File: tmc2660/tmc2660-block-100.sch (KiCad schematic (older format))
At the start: 18 parts, among them J100 0R, M100 Mount, M101 Mount, P100 Motor, U100 TMC2660

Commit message: Wire up quad according to new MISO/MOSI sequence.
- Also, add basic STEP/DIR and a capacitor.
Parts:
- added C?: 100u, Capacitors_THT:CP_Radial_D10.0mm_P5.00mm, symbol device:CP
- renumbered C101 to C100, C100 to C101, C103 to C102, C102 to C103, C106 to C105, C107 to C106, C105 to C107, R101 to R100, R100 to R101, R103 to R102, R102 to R103
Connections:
- net labels added: START_MOSI
- net labels removed: GLOBAL_MISO
- wire segments 51 -> 50
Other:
- note added: "Jumper on\nhighest popuplated"
- note removed: "Optional"
- moved on the sheet: J100
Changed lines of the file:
@@
 EESchema Schematic File Version 4
-LIBS:tmc2660-mono-cache
+LIBS:tmc2660-quad-cache
 EELAYER 26 0
 EELAYER END
 $Descr A4 11693 8268
 encoding utf-8
-Sheet 2 2
+Sheet 2 5
 Title ""
 Date ""
@@
 $EndDescr
 $Comp
-L device:C C102
+L device:C C103
 U 1 1 5A0CA5B9
 P 4250 2250
-F 0 "C102" H 4275 2350 50  0000 L CNN
+F 0 "C103" H 4275 2350 50  0000 L CNN
 F 1 "10u" H 4275 2150 50  0000 L CNN
 F 2 "Capacitors_SMD:C_1206" H 4288 2100 30  0001 C CNN
@@
 $EndComp
 $Comp
-L device:C C103
+L device:C C102
 U 1 1 5A0CA5C0
 P 4250 3100
-F 0 "C103" H 4275 3200 50  0000 L CNN
+F 0 "C102" H 4275 3200 50  0000 L CNN
 F 1 "10u" H 4275 3000 50  0000 L CNN
 F 2 "Capacitors_SMD:C_1206" H 4288 2950 30  0001 C CNN
@@
 $EndComp
 $Comp
-L device:C C106
+L device:C C105
 U 1 1 5A0CA5D3
 P 2900 1800
-F 0 "C106" H 2650 1900 50  0000 L CNN
+F 0 "C105" H 2650 1900 50  0000 L CNN
 F 1 "100n" H 2700 1700 50  0000 L CNN
 F 2 "Capacitors_SMD:C_0805" H 2938 1650 30  0001 C CNN
@@
 Connection ~ 3400 3150
 $Comp
-L device:R R102
+L device:R R103
 U 1 1 5A0CA5F8
 P 3550 2700
-F 0 "R102" V 3650 2700 50  0000 C CNN
+F 0 "R103" V 3650 2700 50  0000 C CNN
 F 1 "10R" V 3550 2700 50  0000 C CNN
 F 2 "Resistors_SMD:R_0603" V 3480 2700 30  0001 C CNN
@@
 $EndComp
 $Comp
-L device:R R103
+L device:R R102
 U 1 1 5A0CA5FF
 P 3550 3550
-F 0 "R103" V 3450 3550 50  0000 C CNN
+F 0 "R102" V 3450 3550 50  0000 C CNN
 F 1 "10R" V 3550 3550 50  0000 C CNN
 F 2 "Resistors_SMD:R_0603" V 3480 3550 30  0001 C CNN
@@
 $EndComp
 $Comp
-L device:C C107
+L device:C C106
 U 1 1 5A0CA648
 P 2250 3700
-F 0 "C107" H 1950 3700 50  0000 L CNN
+F 0 "C106" H 1950 3700 50  0000 L CNN
 F 1 "100n" H 2050 3600 50  0000 L CNN
 F 2 "Capacitors_SMD:C_0603" H 2288 3550 30  0001 C CNN
@@
 $EndComp
 Wire Wire Line
-	1500 2150 2350 2150
+	2050 2150 2350 2150
 Wire Wire Line
 	2350 3500 2300 3500
@@
 	2300 3500 2300 3550
 Wire Wire Line
-	2300 3550 2000 3550
+	2000 3550 2300 3550
 $Comp
 L power:GND #PWR0109
@@
 $EndComp
 $Comp
-L device:R R101
+L device:R R100
 U 1 1 5A0CA66C
 P 3950 3700
-F 0 "R101" V 3850 3650 50  0000 C CNN
+F 0 "R100" V 3850 3650 50  0000 C CNN
 F 1 "0.075" V 3950 3700 50  0000 C CNN
 F 2 "Resistors_SMD:R_2512" V 3880 3700 30  0001 C CNN
@@
 $EndComp
 $Comp
-L device:R R100
+L device:R R101
 U 1 1 5A0CA673
 P 3950 2850
-F 0 "R100" V 3850 2850 50  0000 C CNN
+F 0 "R101" V 3850 2850 50  0000 C CNN
 F 1 "0.075" V 3950 2850 50  0000 C CNN
 F 2 "Resistors_SMD:R_2512" V 3880 2850 30  0001 C CNN
@@
 	2250 2250 2350 2250
 $Comp
-L device:C_Small C100
+L device:C_Small C101
 U 1 1 5A0CA67B
 P 3950 2700
-F 0 "C100" V 3800 2600 50  0000 L CNN
+F 0 "C101" V 3800 2600 50  0000 L CNN
 F 1 "10n" V 3900 2750 50  0000 L CNN
 F 2 "Capacitors_SMD:C_0603" H 3988 2550 30  0001 C CNN
@@
 	3400 2450 3600 2450
 $Comp
-L device:C_Small C101
+L device:C_Small C100
 U 1 1 5A0CA683
 P 3950 3550
-F 0 "C101" V 4000 3600 50  0000 L CNN
+F 0 "C100" V 4000 3600 50  0000 L CNN
 F 1 "10n" V 4000 3350 50  0000 L CNN
 F 2 "Capacitors_SMD:C_0603" H 3988 3400 30  0001 C CNN
@@
 DIR
 Wire Wire Line
-	1250 2400 2350 2400
+	1850 2400 2350 2400
 Wire Wire Line
 	2350 2500 1250 2500
@@
 Connection ~ 3800 2700
 $Comp
-L device:CP C105
+L device:CP C107
 U 1 1 5A0CA6BD
 P 3500 1700
-F 0 "C105" H 3525 1800 50  0000 L CNN
+F 0 "C107" H 3525 1800 50  0000 L CNN
 F 1 "100u" H 3400 1900 50  0000 L CNN
 F 2 "Capacitors_THT:CP_Radial_D10.0mm_P5.00mm" H 3538 1550 30  0001 C CNN
@@
 	3200 1850 3500 1850
 Connection ~ 3350 1850
-Text Notes 1600 2350 0    60   ~ 0
-Optional
+Text Notes 600  2400 0    51   ~ 0
+Jumper on\nhighest popuplated
 Text HLabel 3750 1550 2    60   Input ~ 0
 VMot
@@
 Text HLabel 2000 3550 0    60   Input ~ 0
 VCC
-Text HLabel 1500 2150 0    60   Input ~ 0
+Text HLabel 2050 2150 0    60   Input ~ 0
 ~EN
 $Comp
 L device:R J100
 U 1 1 5A0CA6C8
-P 1400 2300
-F 0 "J100" V 1450 2100 50  0000 C CNN
-F 1 "0R" V 1400 2300 50  0000 C CNN
-F 2 "Resistors_SMD:R_0603" V 1330 2300 30  0001 C CNN
-F 3 "" H 1400 2300 30  0000 C CNN
-	1    1400 2300
-	0    -1   -1   0
-$EndComp
-Text HLabel 1250 2300 0    60   Input ~ 0
-GLOBAL_MISO
-Text HLabel 1250 2400 0    60   Input ~ 0
+P 1450 2350
+F 0 "J100" H 1550 2500 50  0000 C CNN
+F 1 "0R" V 1450 2350 50  0000 C CNN
+F 2 "Resistors_SMD:R_0603" V 1380 2350 30  0001 C CNN
+F 3 "" H 1450 2350 30  0000 C CNN
+	1    1450 2350
+	1    0    0    -1
+$EndComp
+Text HLabel 1250 2200 0    60   Input ~ 0
+START_MOSI
+Text HLabel 1850 2400 0    60   Input ~ 0
 MISO
-Wire Wire Line
-	1550 2300 1600 2300
-Wire Wire Line
-	1600 2300 1600 2400
-Connection ~ 1600 2400
 Text HLabel 1250 2500 0    60   Input ~ 0
 MOSI
@@
 	1    0    0    -1
 $EndComp
+Wire Wire Line
+	1250 2200 1450 2200
+Connection ~ 1450 2500
+$Comp
+L device:CP C?
+U 1 1 5A13AFA9
+P 950 650
+F 0 "C?" H 975 750 50  0000 L CNN
+F 1 "100u" H 850 850 50  0000 L CNN
+F 2 "Capacitors_THT:CP_Radial_D10.0mm_P5.00mm" H 988 500 30  0001 C CNN
+F 3 "" H 950 650 60  0000 C CNN
+	1    950  650
+	1    0    0    -1
+$EndComp

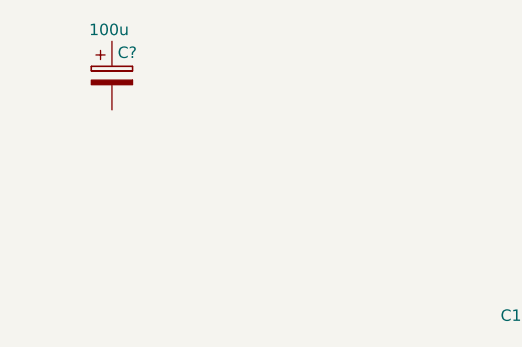
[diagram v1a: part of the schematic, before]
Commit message: Initial version of PCB with cloned template components.
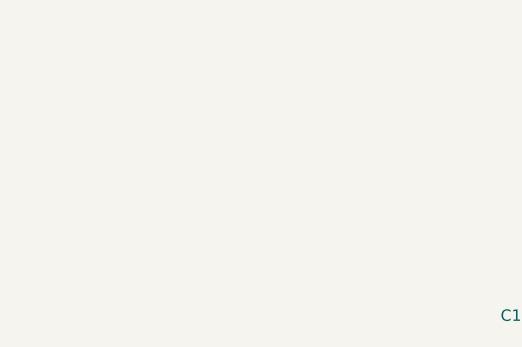
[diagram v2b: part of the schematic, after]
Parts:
- removed C?: 100u, Capacitors_THT:CP_Radial_D10.0mm_P5.00mm, symbol device:CP
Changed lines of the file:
@@
 	1250 2200 1450 2200
 Connection ~ 1450 2500
-$Comp
-L device:CP C?
-U 1 1 5A13AFA9
-P 950 650
-F 0 "C?" H 975 750 50  0000 L CNN
-F 1 "100u" H 850 850 50  0000 L CNN
-F 2 "Capacitors_THT:CP_Radial_D10.0mm_P5.00mm" H 988 500 30  0001 C CNN
-F 3 "" H 950 650 60  0000 C CNN
-	1    950  650
-	1    0    0    -1
-$EndComp
 $EndSCHEMATC

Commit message: Update tmc2660-quad with new template.
o Start out with a tmc2660-quad-baseline that is filled
  in with zones and tracks from the template.
o The separation from baseline and template allows faster
  updates later.
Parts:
- C102, C103: Voltage (none) -> 50V
- C104: footprint Capacitors_SMD:C_0805 -> Capacitors_SMD:C_0603; Voltage (none) -> 50V
- C105: footprint Capacitors_SMD:C_0805 -> Capacitors_SMD:C_0603; Voltage (none) -> 16V
- C106, C108: Voltage (none) -> 16V
- C107: value 100u -> 180u; footprint Capacitors_THT:CP_Radial_D10.0mm_P5.00mm -> Capacitors_THT:CP_Radial_D8.0mm_P3.50mm; DigiKey (none) -> 565-3911-ND; Voltage (none) -> 35V
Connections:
- net labels added: VHS
- wire segments 50 -> 44
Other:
- moved on the sheet: C100, C101, C102, C103, C105, P100, R100, R101, R102, R103

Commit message: Integrate grounded mounting hole.
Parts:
- C102, C103: DigiKey (none) -> 1276-6736-1-ND
- C104: footprint Capacitors_SMD:C_0603 -> Capacitors_SMD:C_0805; DigiKey (none) -> 1276-2450-2-ND
- C105, C106: footprint Capacitors_SMD:C_0603 -> Capacitors_SMD:C_0805; DigiKey (none) -> 1276-2450-2-ND; Voltage 16V -> >= 16V
- M101: footprint Mounting_Holes:MountingHole_2.7mm_M2.5 -> Mounting_Holes:MountingHole_2.7mm_M2.5_Pad; symbol Mechanical:Mounting_Hole -> Mechanical:Mounting_Hole_PAD
- R100, R101: Alternative 100mOhm (none) -> CRM2512-JX-R100ELFCT-ND; DigiKey (none) -> CSRN2512FK75L0CT-ND
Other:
- note added: "Sense Resistors alternatively\nalso with 100mOhm"
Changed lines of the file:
@@
 EESchema Schematic File Version 4
-LIBS:tmc2660-mono-cache
 EELAYER 26 0
 EELAYER END
@@
 F 3 "" H 4400 2300 60  0000 C CNN
 F 4 "50V" H 4400 2300 60  0001 C CNN "Voltage"
+F 5 "1276-6736-1-ND" H 4400 2300 60  0001 C CNN "DigiKey"
 	1    4400 2300
 	1    0    0    -1
@@
 F 3 "" H 4100 2300 60  0000 C CNN
 F 4 "50V" H 4100 2300 60  0001 C CNN "Voltage"
+F 5 "1276-6736-1-ND" H 4100 2300 60  0001 C CNN "DigiKey"
 	1    4100 2300
 	1    0    0    -1
@@
 F 0 "C105" H 2800 2000 50  0000 L CNN
 F 1 "100n" H 2700 1800 50  0000 L CNN
-F 2 "Capacitors_SMD:C_0603" H 2938 1550 30  0001 C CNN
+F 2 "Capacitors_SMD:C_0805" H 2938 1550 30  0001 C CNN
 F 3 "" H 2900 1700 60  0000 C CNN
-F 4 "16V" H 2900 1700 60  0001 C CNN "Voltage"
+F 4 ">= 16V" H 2900 1700 60  0001 C CNN "Voltage"
+F 5 "1276-2450-2-ND" H 2900 1700 60  0001 C CNN "DigiKey"
 	1    2900 1700
 	1    0    0    -1
@@
 F 0 "C104" H 3150 2000 50  0000 L CNN
 F 1 "100n" H 3150 1900 50  0000 L CNN
-F 2 "Capacitors_SMD:C_0603" H 3238 1550 30  0001 C CNN
+F 2 "Capacitors_SMD:C_0805" H 3238 1550 30  0001 C CNN
 F 3 "" H 3200 1700 60  0000 C CNN
 F 4 "50V" H 3200 1700 60  0001 C CNN "Voltage"
+F 5 "1276-2450-2-ND" H 3200 1700 60  0001 C CNN "DigiKey"
 	1    3200 1700
 	1    0    0    -1
@@
 F 0 "C106" H 1950 3700 50  0000 L CNN
 F 1 "100n" H 2050 3600 50  0000 L CNN
-F 2 "Capacitors_SMD:C_0603" H 2288 3550 30  0001 C CNN
+F 2 "Capacitors_SMD:C_0805" H 2288 3550 30  0001 C CNN
 F 3 "" H 2250 3700 60  0000 C CNN
-F 4 "16V" H 2250 3700 60  0001 C CNN "Voltage"
+F 4 ">= 16V" H 2250 3700 60  0001 C CNN "Voltage"
+F 5 "1276-2450-2-ND" H 2250 3700 60  0001 C CNN "DigiKey"
 	1    2250 3700
 	1    0    0    -1
@@
 F 2 "Resistors_SMD:R_2512" V 4330 3500 30  0001 C CNN
 F 3 "" H 4400 3500 30  0000 C CNN
+F 4 "CSRN2512FK75L0CT-ND" H 4400 3500 60  0001 C CNN "DigiKey"
+F 5 "CRM2512-JX-R100ELFCT-ND" H 4400 3500 60  0001 C CNN "Alternative 100mOhm"
 	1    4400 3500
 	-1   0    0    1
@@
 F 2 "Resistors_SMD:R_2512" V 4330 2950 30  0001 C CNN
 F 3 "" H 4400 2950 30  0000 C CNN
+F 4 "CSRN2512FK75L0CT-ND" H 4400 2950 60  0001 C CNN "DigiKey"
+F 5 "CRM2512-JX-R100ELFCT-ND" H 4400 2950 60  0001 C CNN "Alternative 100mOhm"
 	1    4400 2950
 	1    0    0    -1
@@
 L Mechanical:Mounting_Hole M100
 U 1 1 5A0FBC47
-P 1250 4300
-F 0 "M100" H 1308 4420 50  0000 L CNN
-F 1 "Mount" H 1308 4329 50  0000 L CNN
-F 2 "Mounting_Holes:MountingHole_2.7mm_M2.5" H 1450 4300 50  0001 C CNN
-F 3 "~" H 1450 4300 50  0001 C CNN
-	1    1250 4300
-	1    0    0    -1
-$EndComp
-$Comp
-L Mechanical:Mounting_Hole M101
+P 1250 4250
+F 0 "M100" H 1150 4400 50  0000 L CNN
+F 1 "Mount" H 1308 4279 50  0000 L CNN
+F 2 "Mounting_Holes:MountingHole_2.7mm_M2.5" H 1450 4250 50  0001 C CNN
+F 3 "~" H 1450 4250 50  0001 C CNN
+	1    1250 4250
+	1    0    0    -1
+$EndComp
+$Comp
+L Mechanical:Mounting_Hole_PAD M101
 U 1 1 5A0FBD0F
 P 1650 4300
-F 0 "M101" H 1708 4420 50  0000 L CNN
+F 0 "M101" H 1550 4500 50  0000 L CNN
 F 1 "Mount" H 1708 4329 50  0000 L CNN
-F 2 "Mounting_Holes:MountingHole_2.7mm_M2.5" H 1850 4300 50  0001 C CNN
+F 2 "Mounting_Holes:MountingHole_2.7mm_M2.5_Pad" H 1850 4300 50  0001 C CNN
 F 3 "~" H 1850 4300 50  0001 C CNN
 	1    1650 4300
@@
 Text Label 2900 1950 1    39   ~ 0
 VHS
+Text Notes 4500 3750 0    51   ~ 0
+Sense Resistors alternatively\nalso with 100mOhm
+$Comp
+L power:GND #PWR?
+U 1 1 5A1C342B
+P 1650 4400
+F 0 "#PWR?" H 1650 4150 50  0001 C CNN
+F 1 "GND" H 1650 4250 50  0000 C CNN
+F 2 "" H 1650 4400 60  0000 C CNN
+F 3 "" H 1650 4400 60  0000 C CNN
+	1    1650 4400
+	1    0    0    -1
+$EndComp
 $EndSCHEMATC

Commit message: Move VMOT 100nF input stabilisator for VHS voltage regulator close to pin.
o Re-number the 100nF capacitors that they show up in an increasing numbers
o Use opportunity to move silkscreen of 10uF capacitors out of via's harms way.
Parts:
- renumbered C105 to C104, C104 to C105
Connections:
- wire segments 44 -> 63
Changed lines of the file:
@@
 EESchema Schematic File Version 4
-LIBS:tmc2660-quad-cache
 EELAYER 26 0
 EELAYER END
 $Descr A4 11693 8268
 encoding utf-8
-Sheet 2 5
+Sheet 2 2
 Title ""
 Date ""
@@
 $EndComp
 $Comp
-L device:C C105
+L device:C C104
 U 1 1 5A0CA5D3
 P 2900 1700
-F 0 "C105" H 2800 2000 50  0000 L CNN
+F 0 "C104" H 2800 2000 50  0000 L CNN
 F 1 "100n" H 2700 1800 50  0000 L CNN
 F 2 "Capacitors_SMD:C_0805" H 2938 1550 30  0001 C CNN
@@
 $EndComp
 $Comp
-L device:C C104
+L device:C C105
 U 1 1 5A0CA5DE
 P 3200 1700
-F 0 "C104" H 3150 2000 50  0000 L CNN
+F 0 "C105" H 3150 2000 50  0000 L CNN
 F 1 "100n" H 3150 1900 50  0000 L CNN
 F 2 "Capacitors_SMD:C_0805" H 3238 1550 30  0001 C CNN
@@
 Connection ~ 3050 1550
 Wire Wire Line
-	2700 3800 2900 3800
+	2700 3800 2800 3800
 Connection ~ 2800 3800
 Connection ~ 3400 2250
@@
 	3400 2250 3600 2250
 Wire Wire Line
-	3400 3300 3400 3450
+	3400 3300 3400 3350
 Connection ~ 3400 3350
 Wire Wire Line
-	3400 3050 3400 3200
+	3400 3050 3400 3100
 Connection ~ 3400 3100
 Wire Wire Line
-	3400 2450 3400 2600
+	3400 2450 3400 2500
 Connection ~ 3400 2500
 Wire Wire Line
-	3400 2200 3400 2350
+	3400 2200 3400 2250
 Connection ~ 3400 2300
 Wire Wire Line
@@
 	2300 3500 2300 3550
 Wire Wire Line
-	2000 3550 2300 3550
+	2000 3550 2250 3550
 Wire Wire Line
 	2250 2250 2350 2250
 Wire Wire Line
 	3400 2450 3600 2450
-Connection ~ 3400 3300
 Connection ~ 3400 3400
 Wire Wire Line
-	3400 3550 3800 3550
+	3400 3550 3750 3550
 Wire Wire Line
 	3400 2700 3800 2700
 Wire Wire Line
-	3400 2800 4400 2800
-Connection ~ 3400 3050
+	3400 2800 4250 2800
 Wire Wire Line
 	2350 2850 1950 2850
@@
 	1850 2400 2350 2400
 Wire Wire Line
-	1250 2500 2350 2500
+	1250 2500 1450 2500
 Wire Wire Line
 	2350 2600 1250 2600
@@
 Connection ~ 3200 1550
 Wire Wire Line
-	3200 1850 3500 1850
+	3200 1850 3350 1850
 Connection ~ 3350 1850
 Connection ~ 3500 1550
 Wire Wire Line
-	2900 1550 3750 1550
+	2900 1550 3050 1550
 Wire Wire Line
 	3400 3100 3600 3100
@@
 Connection ~ 3800 2700
 Wire Wire Line
-	4400 3100 4400 3350
+	4400 3100 4400 3200
 Wire Wire Line
 	4400 3200 4600 3200
 Connection ~ 4400 3200
 Wire Wire Line
-	3400 3650 4400 3650
+	3400 3650 4200 3650
 Wire Wire Line
 	4100 3550 4200 3550
@@
 Wire Wire Line
 	4100 2450 4400 2450
-Connection ~ 4400 2450
 Wire Wire Line
 	2900 1850 2900 1950
@@
 Sense Resistors alternatively\nalso with 100mOhm
 $Comp
-L power:GND #PWR03
+L power:GND #PWR?
 U 1 1 5A1C342B
 P 1650 4400
-F 0 "#PWR03" H 1650 4150 50  0001 C CNN
+F 0 "#PWR?" H 1650 4150 50  0001 C CNN
 F 1 "GND" H 1650 4250 50  0000 C CNN
 F 2 "" H 1650 4400 60  0000 C CNN
@@
 	1    0    0    -1
 $EndComp
+Wire Wire Line
+	3050 1550 3200 1550
+Wire Wire Line
+	2800 3800 2900 3800
+Wire Wire Line
+	3400 2250 3400 2300
+Wire Wire Line
+	3400 2550 3400 2600
+Wire Wire Line
+	3400 3150 3400 3200
+Wire Wire Line
+	3400 3350 3400 3400
+Wire Wire Line
+	3400 3100 3400 3150
+Wire Wire Line
+	3400 2500 3400 2550
+Wire Wire Line
+	3400 2300 3400 2350
+Wire Wire Line
+	2250 3550 2300 3550
+Wire Wire Line
+	3400 3400 3400 3450
+Wire Wire Line
+	3200 1550 3500 1550
+Wire Wire Line
+	3350 1850 3500 1850
+Wire Wire Line
+	3500 1550 3750 1550
+Wire Wire Line
+	1450 2500 2350 2500
+Wire Wire Line
+	4250 2800 4400 2800
+Wire Wire Line
+	4400 3200 4400 3350
+Wire Wire Line
+	4200 3650 4400 3650
+Wire Wire Line
+	3750 3550 3800 3550
 $EndSCHEMATC
